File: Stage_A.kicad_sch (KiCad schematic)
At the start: 25 parts, among them U1 SKY13575-639LF, U10 SKY13575-639LF, U11 SKY13575-639LF, U12 SKY13575-639LF, U2 SKY13575-639LF, U3 SKY13575-639LF, U4 SKY13575-639LF, U5 SKY13575-639LF, U6 SKY13575-639LF, U7 SKY13575-639LF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

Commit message: skdja7rkweg
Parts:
- W1, W2, W3, W4, W5, W6: value ~ -> (none)
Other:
- sheet FAN_A ports: added VCC; removed none
- sheet FAN_B ports: added VCC; removed none
- sheet FAN_C ports: added VCC; removed none
- sheet FAN_D ports: added VCC; removed none
- sheet FAN_E ports: added VCC; removed none
- sheet FAN_F ports: added VCC; removed none

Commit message: moving along
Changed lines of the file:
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@@
 	(text "Microstrip Wilkinson power dividers"
 		(exclude_from_sim no)
-		(at 60.96 55.88 0)
+		(at 71.12 35.56 0)
 		(effects
 			(font
@@
 		(pts
 			(xy 200.66 53.34) (xy 187.96 53.34)
-		)
-		(stroke
-			(width 0)
-			(type default)
-		)
-	)
-	(wire
-		(pts
-			(xy 185.42 63.5) (xy 187.96 63.5)
 		)
 		(stroke
@@
 		)
 	)
+	(netclass_flag ""
+		(length 2.54)
+		(shape round)
+		(at 114.3 63.5 0)
+		(fields_autoplaced yes)
+		(effects
+			(font
+				(size 1.27 1.27)
+			)
+			(justify left bottom)
+		)
+		(property "Net Class" "50 ohm"
+			(at 114.9985 60.96 0)
+			(show_name no)
+			(do_not_autoplace no)
+			(effects
+				(font
+					(size 1.27 1.27)
+				)
+				(justify left)
+			)
+		)
+		(property "Component Class" ""
+			(at 113.03 -7.62 0)
+			(show_name no)
+			(do_not_autoplace no)
+			(effects
+				(font
+					(size 1.27 1.27)
+					(italic yes)
+				)
+			)
+		)
+	)
+	(netclass_flag ""
+		(length 2.54)
+		(shape round)
+		(at 116.84 93.98 0)
+		(fields_autoplaced yes)
+		(effects
+			(font
+				(size 1.27 1.27)
+			)
+			(justify left bottom)
+		)
+		(property "Net Class" "50 ohm"
+			(at 117.5385 91.44 0)
+			(show_name no)
+			(do_not_autoplace no)
+			(effects
+				(font
+					(size 1.27 1.27)
+				)
+				(justify left)
+			)
+		)
+		(property "Component Class" ""
+			(at 115.57 22.86 0)
+			(show_name no)
+			(do_not_autoplace no)
+			(effects
+				(font
+					(size 1.27 1.27)
+					(italic yes)
+				)
+			)
+		)
+	)
+	(netclass_flag ""
+		(length 2.54)
+		(shape round)
+		(at 118.11 121.92 0)
+		(fields_autoplaced yes)
+		(effects
+			(font
+				(size 1.27 1.27)
+			)
+			(justify left bottom)
+		)
+		(property "Net Class" "50 ohm"
+			(at 118.8085 119.38 0)
+			(show_name no)
+			(do_not_autoplace no)
+			(effects
+				(font
+					(size 1.27 1.27)
+				)
+				(justify left)
+			)
+		)
+		(property "Component Class" ""
+			(at 116.84 50.8 0)
+			(show_name no)
+			(do_not_autoplace no)
+			(effects
+				(font
+					(size 1.27 1.27)
+					(italic yes)
+				)
+			)
+		)
+	)
+	(netclass_flag ""
+		(length 2.54)
+		(shape round)
+		(at 115.57 73.66 0)
+		(fields_autoplaced yes)
+		(effects
+			(font
+				(size 1.27 1.27)
+			)
+			(justify left bottom)
+		)
+		(property "Net Class" "50 ohm"
+			(at 116.2685 71.12 0)
+			(show_name no)
+			(do_not_autoplace no)
+			(effects
+				(font
+					(size 1.27 1.27)
+				)
+				(justify left)
+			)
+		)
+		(property "Component Class" ""
+			(at 114.3 2.54 0)
+			(show_name no)
+			(do_not_autoplace no)
+			(effects
+				(font
+					(size 1.27 1.27)
+					(italic yes)
+				)
+			)
+		)
+	)
+	(netclass_flag ""
+		(length 2.54)
+		(shape round)
+		(at 118.11 111.76 0)
+		(fields_autoplaced yes)
+		(effects
+			(font
+				(size 1.27 1.27)
+			)
+			(justify left bottom)
+		)
+		(property "Net Class" "50 ohm"
+			(at 118.8085 109.22 0)
+			(show_name no)
+			(do_not_autoplace no)
+			(effects
+				(font
+					(size 1.27 1.27)
+				)
+				(justify left)
+			)
+		)
+		(property "Component Class" ""
+			(at 116.84 40.64 0)
+			(show_name no)
+			(do_not_autoplace no)
+			(effects
+				(font
+					(size 1.27 1.27)
+					(italic yes)
+				)
+			)
+		)
+	)
+	(netclass_flag ""
+		(length 2.54)
+		(shape round)
+		(at 115.57 86.36 0)
+		(fields_autoplaced yes)
+		(effects
+			(font
+				(size 1.27 1.27)
+			)
+			(justify left bottom)
+		)
+		(property "Net Class" "50 ohm"
+			(at 116.2685 83.82 0)
+			(show_name no)
+			(do_not_autoplace no)
+			(effects
+				(font
+					(size 1.27 1.27)
+				)
+				(justify left)
+			)
+		)
+		(property "Component Class" ""
+			(at 114.3 15.24 0)
+			(show_name no)
+			(do_not_autoplace no)
+			(effects
+				(font
+					(size 1.27 1.27)
+					(italic yes)
+				)
+			)
+		)
+	)

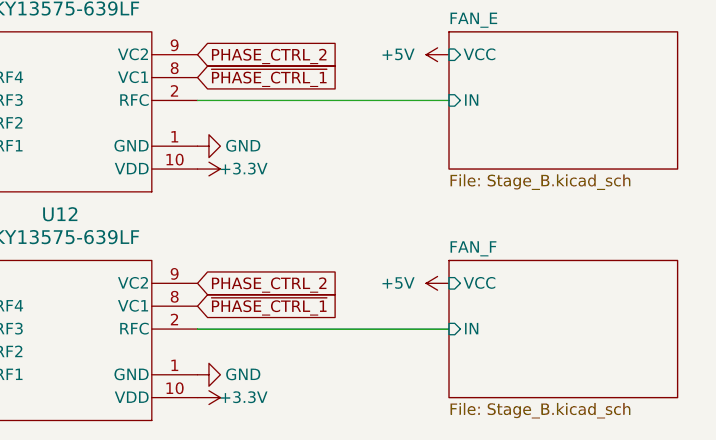
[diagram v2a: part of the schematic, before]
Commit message: 6 layers now
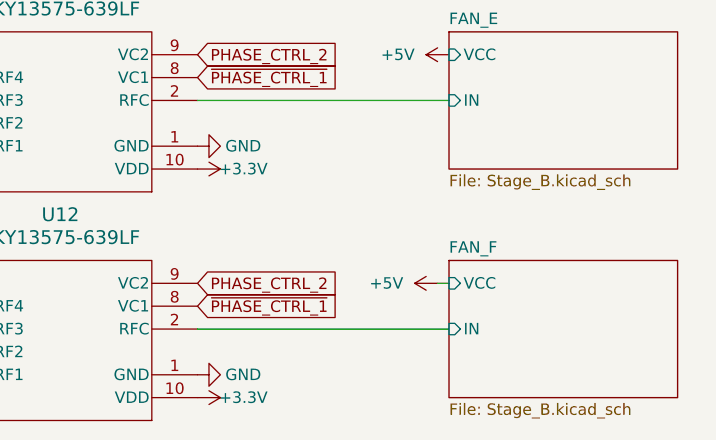
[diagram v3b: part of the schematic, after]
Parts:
- R1, R2, R3, R4, R5, R6, RL1: price (none) -> .04
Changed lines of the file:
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@@
 	(wire
 		(pts
+			(xy 255.27 149.86) (xy 256.54 149.86)
+		)
+		(stroke
+			(width 0)
+			(type default)
+		)
+	)
+	(wire
+		(pts
 			(xy 200.66 152.4) (xy 187.96 152.4)
 		)
@@
 			)
 		)
+		(property "price" ".04"
+			(at 50.8 96.52 0)
+			(hide yes)
+			(show_name no)
+			(do_not_autoplace no)
+			(effects
+				(font
+					(size 1.27 1.27)
+				)
+			)
+		)
 		(pin "1"
 		)
@@
 			)
 		)
+		(property "price" ".04"
+			(at 76.2 139.7 0)
+			(hide yes)
+			(show_name no)
+			(do_not_autoplace no)
+			(effects
+				(font
+					(size 1.27 1.27)
+				)
+			)
+		)
 		(pin "1"
 		)
@@
 			)
 		)
+		(property "price" ".04"
+			(at 76.2 124.46 0)
+			(hide yes)
+			(show_name no)
+			(do_not_autoplace no)
+			(effects
+				(font
+					(size 1.27 1.27)
+				)
+			)
+		)
 		(pin "1"
 		)
@@
 	(symbol
 		(lib_id "power:+5V")
-		(at 256.54 149.86 90)
+		(at 255.27 149.86 90)
 		(mirror x)
 		(unit 1)
@@
 		(fields_autoplaced yes)
 		(property "Reference" "#PWR053"
-			(at 260.35 149.86 0)
+			(at 259.08 149.86 0)
 			(hide yes)
 			(show_name no)
@@
 		)
 		(property "Value" "+5V"
-			(at 252.73 149.8599 90)
+			(at 251.46 149.8599 90)
 			(show_name no)
 			(do_not_autoplace no)
@@
 		)
 		(property "Footprint" ""
-			(at 256.54 149.86 0)
+			(at 255.27 149.86 0)
 			(hide yes)
 			(show_name no)
@@
 		)
 		(property "Datasheet" ""
-			(at 256.54 149.86 0)
+			(at 255.27 149.86 0)
 			(hide yes)
 			(show_name no)
@@
 		)
 		(property "Description" "Power symbol creates a global label with name \"+5V\""
-			(at 256.54 149.86 0)
+			(at 255.27 149.86 0)
 			(hide yes)
 			(show_name no)
@@
 			)
 		)
+		(property "price" ".04"
+			(at 101.6 116.84 0)
+			(hide yes)
+			(show_name no)
+			(do_not_autoplace no)
+			(effects
+				(font
+					(size 1.27 1.27)
+				)
+			)
+		)
 		(pin "1"
 		)
@@
 			)
 		)
+		(property "price" ".04"
+			(at 101.6 68.58 0)
+			(hide yes)
+			(show_name no)
+			(do_not_autoplace no)
+			(effects
+				(font
+					(size 1.27 1.27)
+				)
+			)
+		)
 		(pin "1"
 		)
@@
 			)
 		)
+		(property "price" ".04"
+			(at 101.6 88.9 0)
+			(hide yes)
+			(show_name no)
+			(do_not_autoplace no)
+			(effects
+				(font
+					(size 1.27 1.27)
+				)
+			)
+		)
 		(pin "1"
 		)
@@
 			(hide yes)
 			(show_name no)
+			(do_not_autoplace no)
+			(effects
+				(font
+					(size 1.27 1.27)
+				)
+			)
+		)
+		(property "price" ".04"
+			(at 76.2 76.2 0)
+			(hide yes)
+			(show_name no)

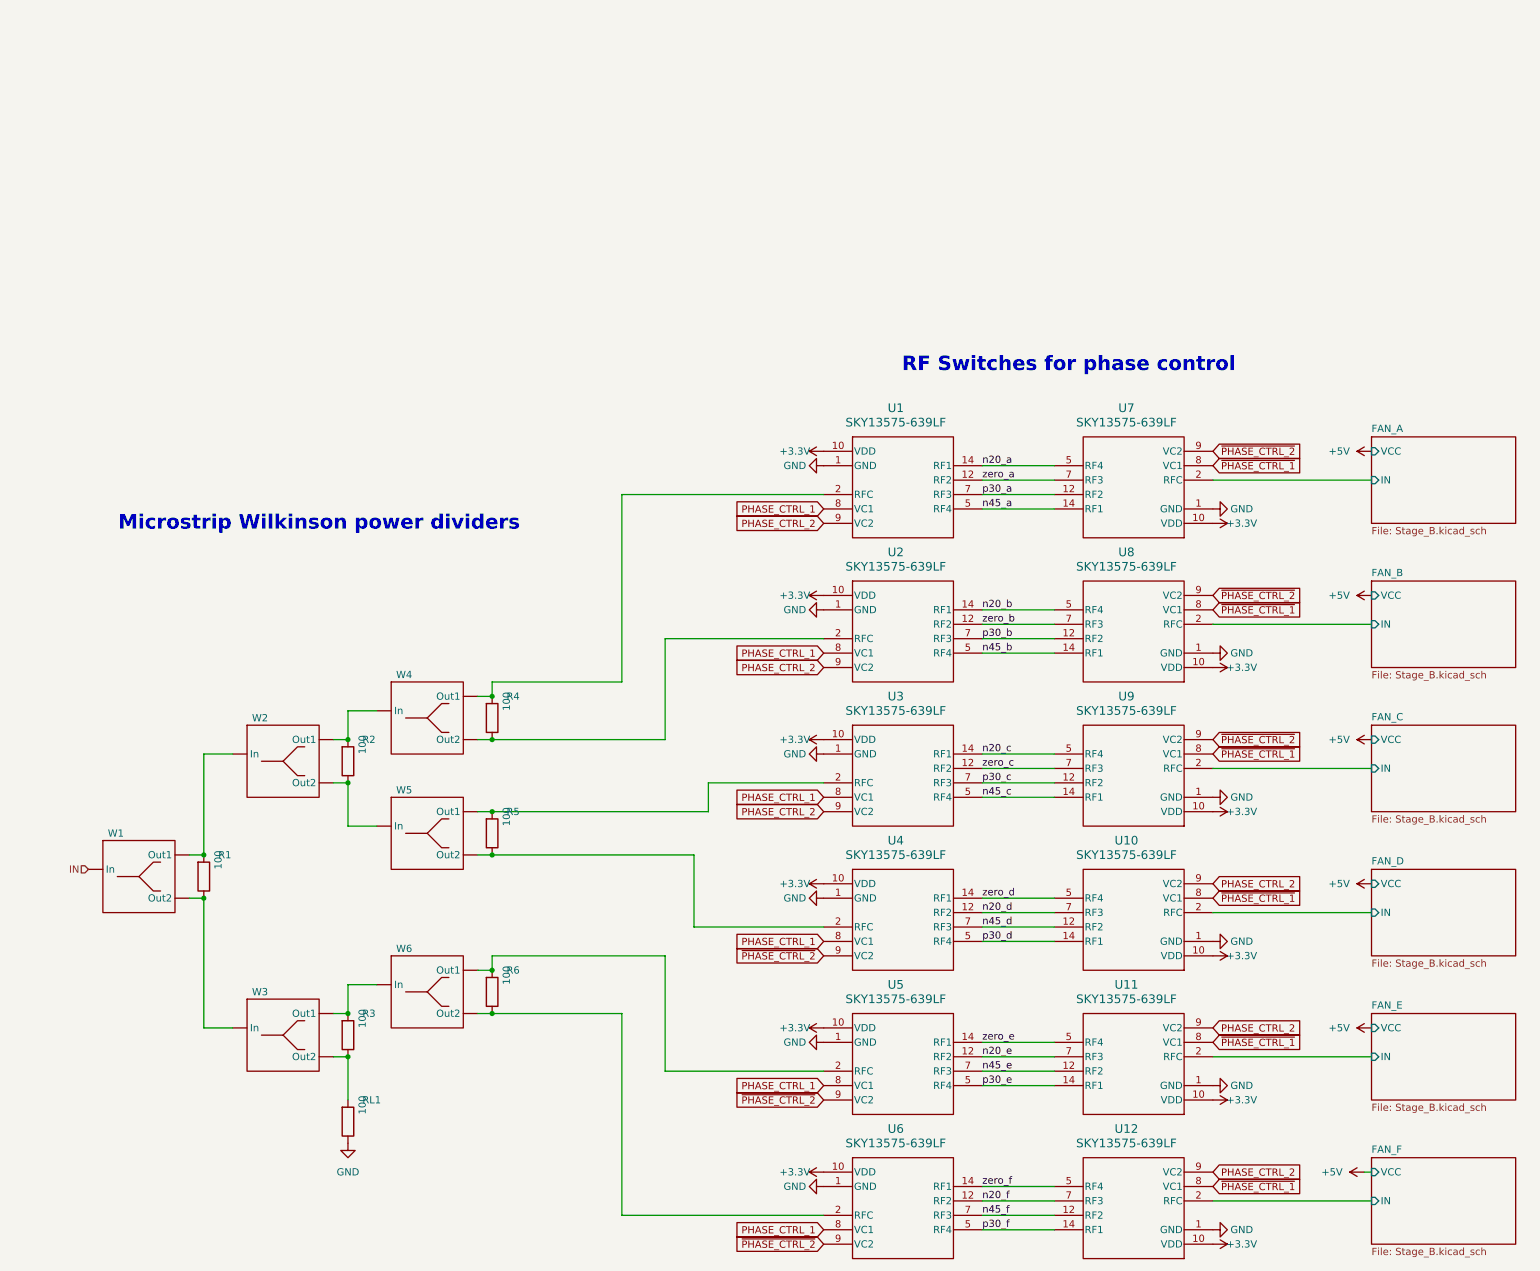
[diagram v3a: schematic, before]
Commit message: completed length matching
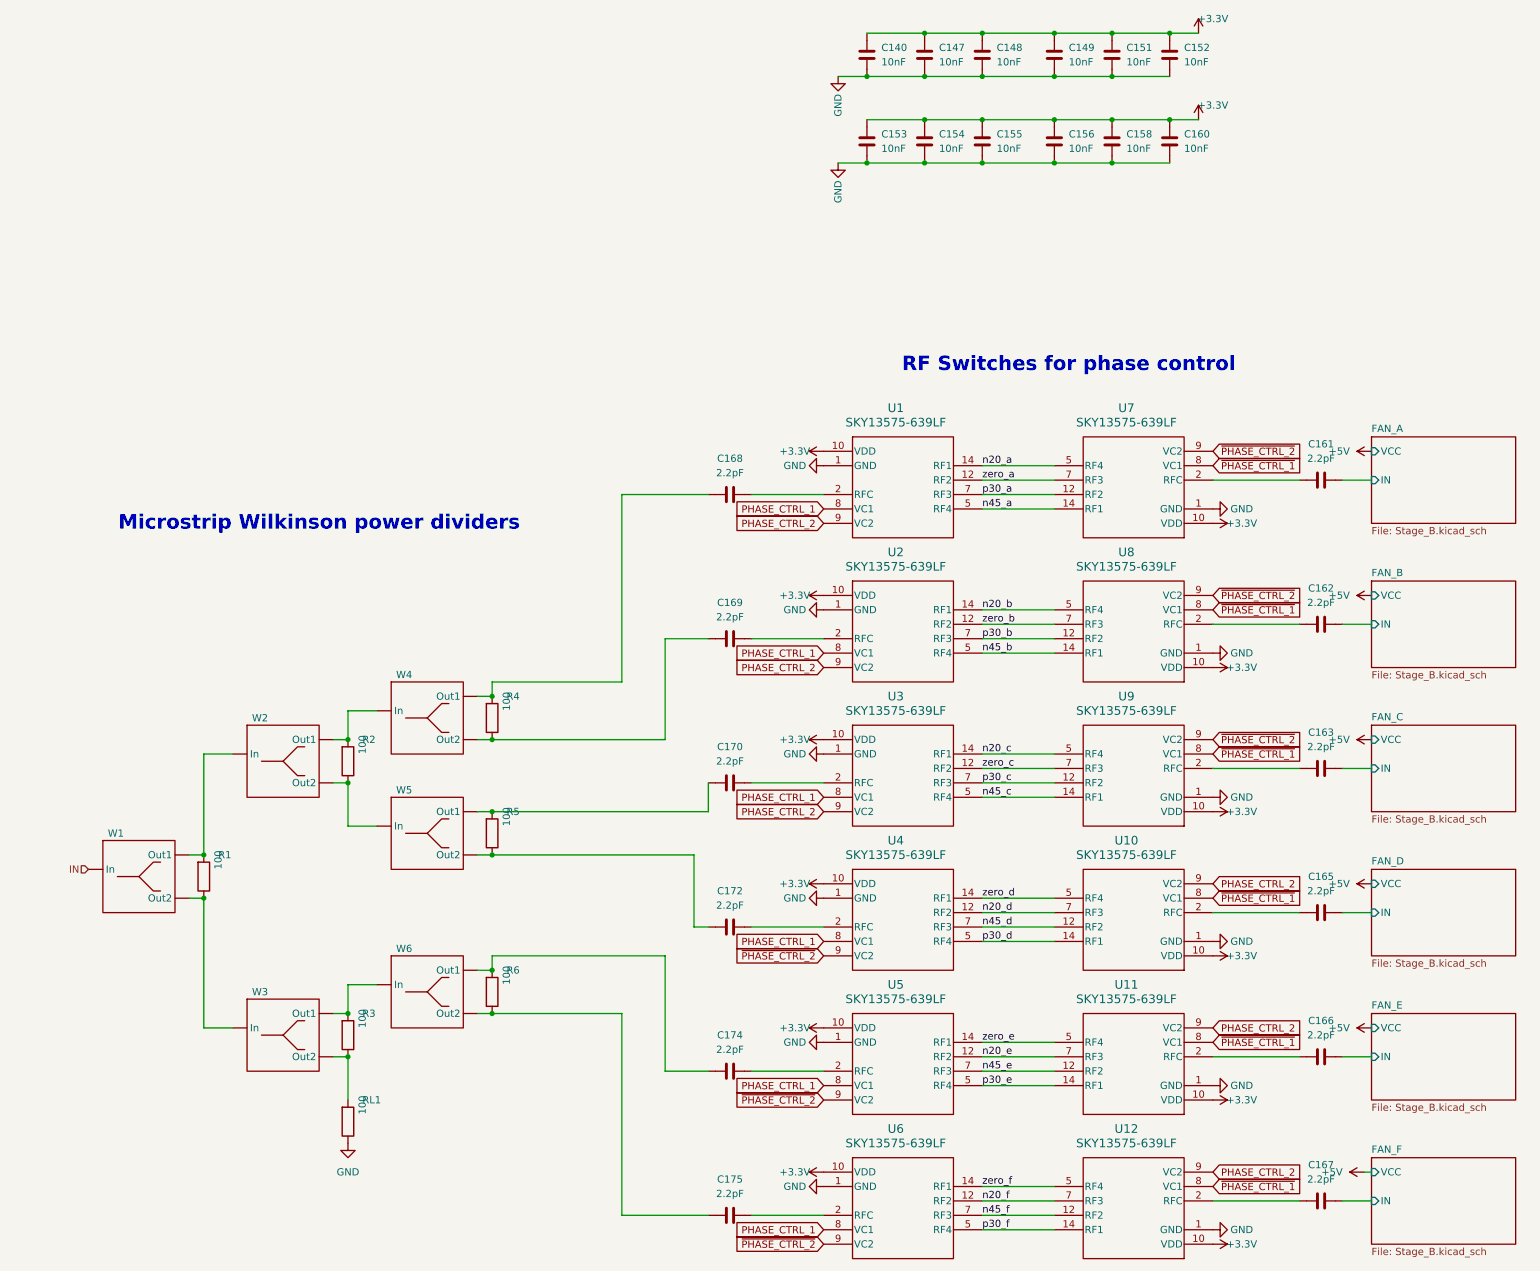
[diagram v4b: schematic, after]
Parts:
- added C140, C147, C148, C149, C151, C152, C153, C154, C155, C156, C158, C160: 10nF, Capacitor_SMD:C_0402_1005Metric, symbol Capacitors:0402_nF010_50V
- added C161, C162, C163, C165, C166, C167, C168, C169, C170, C172, C174, C175: 2.2pF, Capacitor_SMD:C_0402_1005Metric, symbol Capacitors:0402_pF2.2_50V
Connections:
- net +3.3V: now also C140.1, C147.1, C148.1, C149.1, C151.1, C152.1, C153.1, C154.1, C155.1, C156.1, C158.1, C160.1
- net FAN_A/IN: now also C161.2; no longer U7.2 (RFC)
- net FAN_B/IN: now also C162.2; no longer U8.2 (RFC)
- net FAN_C/IN: now also C163.2; no longer U9.2 (RFC)
- net FAN_D/IN: now also C165.2; no longer U10.2 (RFC)
- net FAN_E/IN: now also C166.2; no longer U11.2 (RFC)
- net FAN_F/IN: now also C167.2; no longer U12.2 (RFC)
- net GND: now also C140.2, C147.2, C148.2, C149.2, C151.2, C152.2, C153.2, C154.2, C155.2, C156.2, C158.2, C160.2
- net at R6.1, W6.2 (Out1): now also C174.1; no longer U5.2 (RFC)
- net at R6.2, W6.3 (Out2): now also C175.1; no longer U6.2 (RFC)
- net at R4.1, W4.2 (Out1): now also C168.1; no longer U1.2 (RFC)
- net at R4.2, W4.3 (Out2): now also C169.1; no longer U2.2 (RFC)
- net at R5.1, W5.2 (Out1): now also C170.1; no longer U3.2 (RFC)
- net at R5.2, W5.3 (Out2): now also C172.1; no longer U4.2 (RFC)
- new net: C165.1, U10.2 (RFC)
- new net: C175.2, U6.2 (RFC)
- new net: C161.1, U7.2 (RFC)
- new net: C168.2, U1.2 (RFC)
- new net: C170.2, U3.2 (RFC)
- new net: C174.2, U5.2 (RFC)
- new net: C163.1, U9.2 (RFC)
- new net: C172.2, U4.2 (RFC)
- new net: C169.2, U2.2 (RFC)
- new net: C162.1, U8.2 (RFC)
- new net: C166.1, U11.2 (RFC)
- new net: C167.1, U12.2 (RFC)

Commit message: june_26
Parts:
- C161, C162, C163, C165, C166, C167, C168, C169, C170, C172, C174, C175: symbol Capacitors:0402_pF2.2_50V -> Capacitors:0402_pF002.2_50V; price (none) -> .08
- RL1: value 100 -> 50; symbol Resistors:0402_R100 -> Resistors:0402_R050; DN P100DECT-ND -> TNP49.9DACT-ND; MFR Panasonic Electronic Components -> Vishay Dale; MPN ERA-2AED101X -> TNPW040249R9BEED; price .04 -> .30
- U1, U10, U11, U12, U2, U3, U4, U5, U6, U7, U8, U9: price (none) -> 1.79
- W1, W2, W3, W4, W5, W6: value (none) -> splitter; DNP (none) -> DNP; now not fitted
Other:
- sheet FAN_A ports: added power_det; removed none
